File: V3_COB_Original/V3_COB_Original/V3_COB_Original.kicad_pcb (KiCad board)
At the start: 4 copper layers, 14 x 16 mm, 3 parts, among them J101 Conn_02x35_Counter_Clockwise_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

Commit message: mosbius logo update
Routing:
- net GND: vias 22 -> 21
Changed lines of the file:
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@@
 		)
+	)
+	(gr_line
+		(start 178.1825 86.73625)
+		(end 178.2825 86.84625)
+		(stroke
+			(width 0.05)
+			(type solid)
+		)
+		(layer "F.SilkS")
+	)
+	(gr_line
+		(start 177.852499 86.82625)
+		(end 178.3225 86.416251)
+		(stroke
+			(width 0.05)
+			(type solid)
+		)
+		(layer "F.SilkS")
+	)
+	(gr_line
+		(start 178.1825 86.73625)
+		(end 178.2575 86.67375)
+		(stroke
+			(width 0.05)
+			(type solid)
+		)
+		(layer "F.SilkS")
+	)
+	(gr_line
+		(start 178.0625 86.44625)
+		(end 178.2575 86.67375)
+		(stroke
+			(width 0.05)
+			(type solid)
+		)
+		(layer "F.SilkS")
+	)
+	(gr_line
+		(start 177.9925 86.506705)
+		(end 178.0625 86.44625)
+		(stroke
+			(width 0.05)
+			(type solid)
+		)
+		(layer "F.SilkS")
+	)
+	(gr_line
+		(start 177.8925 86.39625)
+		(end 177.9925 86.50625)
+		(stroke
+			(width 0.05)
+			(type solid)
+		)
+		(layer "F.SilkS")
+	)
+	(gr_arc
+		(start 178.3225 86.41625)
+		(mid 178.804282 86.677927)
+		(end 178.2825 86.84625)
+		(stroke
+			(width 0.05)
+			(type solid)
+		)
+		(layer "F.SilkS")
+	)
+	(gr_arc
+		(start 177.8525 86.82625)
+		(mid 177.370718 86.564573)
+		(end 177.8925 86.39625)
+		(stroke
+			(width 0.05)
+			(type solid)
+		)
+		(layer "F.SilkS")
+	)
+	(gr_line
+		(start 178.13125 86.389375)
+		(end 178.33375 86.623125)
+		(stroke
+			(width 0.05)
+			(type solid)
+		)
+		(layer "F.SilkS")
+	)
+	(gr_line
+		(start 177.849999 86.82)
+		(end 178.32 86.410001)
+		(stroke
+			(width 0.05)
+			(type solid)
+		)
+		(layer "B.SilkS")
+	)
+	(gr_line
+		(start 178.18 86.73)
+		(end 178.255 86.6675)
+		(stroke
+			(width 0.05)
+			(type solid)
+		)
+		(layer "B.SilkS")
+	)
+	(gr_line
+		(start 177.89 86.39)
+		(end 177.99 86.5)
+		(stroke
+			(width 0.05)
+			(type solid)
+		)
+		(layer "B.SilkS")
+	)
+	(gr_arc
+		(start 177.85 86.82)
+		(mid 177.368218 86.558323)
+		(end 177.89 86.39)
+		(stroke
+			(width 0.05)
+			(type solid)
+		)
+		(layer "B.SilkS")
+	)
+	(gr_line
+		(start 178.12875 86.383125)
+		(end 178.33125 86.616875)
+		(stroke
+			(width 0.05)
+			(type solid)
+		)
+		(layer "B.SilkS")
+	)
+	(gr_line
+		(start 178.06 86.44)
+		(end 178.255 86.6675)
+		(stroke
+			(width 0.05)
+			(type solid)
+		)
+		(layer "B.SilkS")
+	)
+	(gr_arc
+		(start 178.32 86.41)
+		(mid 178.801782 86.671677)
+		(end 178.28 86.84)
+		(stroke
+			(width 0.05)
+			(type solid)
+		)
+		(layer "B.SilkS")
+	)
+	(gr_line
+		(start 177.99 86.500455)
+		(end 178.06 86.44)
+		(stroke
+			(width 0.05)
+			(type solid)
+		)
+		(layer "B.SilkS")
+	)
+	(gr_line
+		(start 178.18 86.73)
+		(end 178.28 86.84)
+		(stroke
+			(width 0.05)
+			(type solid)
+		)
+		(layer "B.SilkS")
 	)
 	(gr_rect
@@
 	)
 	(via
-		(at 177.9 86.7)
+		(at 177.3 74.8)
+		(size 0.45)
+		(drill 0.3)
+		(layers "F.Cu" "B.Cu")
+		(net 1)
+	)
+	(via
+		(at 179.355 72.6)
 		(size 0.45)
 		(drill 0.3)
@@
 	)
 	(via
-		(at 177.3 74.8)
-		(size 0.45)
-		(drill 0.3)
-		(layers "F.Cu" "B.Cu")
-		(net 1)
-	)
-	(via
-		(at 179.355 72.6)
+		(at 182.77 87.13)
+		(size 0.45)
+		(drill 0.3)
+		(layers "F.Cu" "B.Cu")
+		(net 1)
+	)
+	(via
+		(at 183.355 80.7)
+		(size 0.45)
+		(drill 0.3)
+		(layers "F.Cu" "B.Cu")
+		(net 1)
+	)
+	(via
+		(at 183.355 82.22)
+		(size 0.45)
+		(drill 0.3)
+		(layers "F.Cu" "B.Cu")
+		(net 1)
+	)
+	(via
+		(at 182.785 82.95)
+		(size 0.45)
+		(drill 0.3)
+		(layers "F.Cu" "B.Cu")
+		(net 1)
+	)
+	(via
+		(at 183.355 76.15)
+		(size 0.45)
+		(drill 0.3)
+		(layers "F.Cu" "B.Cu")
+		(net 1)
+	)
+	(via
+		(at 188.579446 84.025518)
+		(size 0.45)
+		(drill 0.3)
+		(layers "F.Cu" "B.Cu")
+		(net 1)
+	)
+	(via
+		(at 179.58 86.99)
 		(size 0.45)
 		(drill 0.3)
@@
 		(net 1)
 	)
-	(via
-		(at 182.77 87.13)
-		(size 0.45)
-		(drill 0.3)
-		(layers "F.Cu" "B.Cu")
-		(net 1)
-	)
-	(via
-		(at 183.355 80.7)
-		(size 0.45)
-		(drill 0.3)
-		(layers "F.Cu" "B.Cu")
-		(net 1)
-	)
-	(via
-		(at 179.3 86.9)
-		(size 0.45)
-		(drill 0.3)
-		(layers "F.Cu" "B.Cu")
-		(net 1)
-	)
-	(via
-		(at 183.355 82.22)
-		(size 0.45)
-		(drill 0.3)
-		(layers "F.Cu" "B.Cu")
-		(net 1)
-	)
-	(via
-		(at 182.785 82.95)
-		(size 0.45)
-		(drill 0.3)
-		(layers "F.Cu" "B.Cu")
-		(net 1)
-	)
-	(via
-		(at 183.355 76.15)
-		(size 0.45)
-		(drill 0.3)
-		(layers "F.Cu" "B.Cu")
-		(net 1)
-	)
-	(via
-		(at 188.579446 84.025518)
-		(size 0.45)
-		(drill 0.3)
-		(layers "F.Cu" "B.Cu")
-		(net 1)
-	)

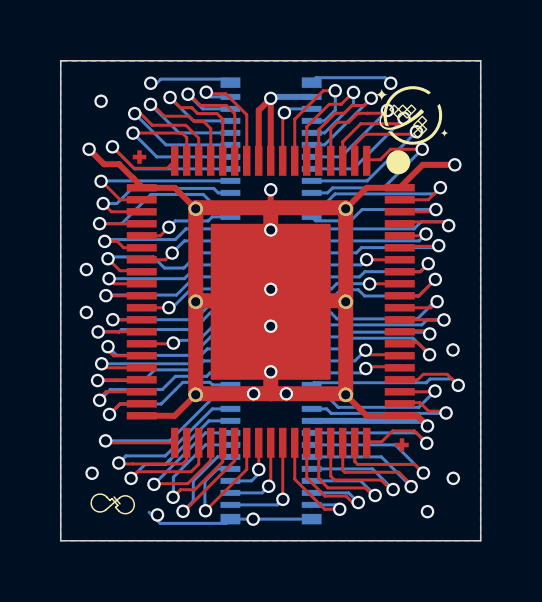
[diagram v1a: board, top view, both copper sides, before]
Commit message: create panel
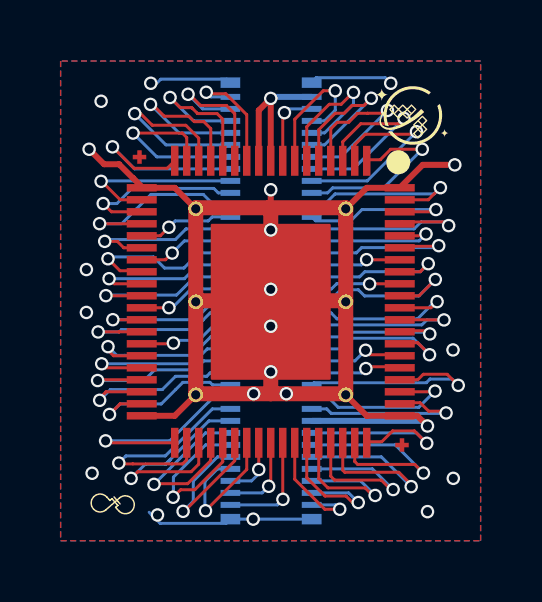
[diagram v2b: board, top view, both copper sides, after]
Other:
- board outline removed
